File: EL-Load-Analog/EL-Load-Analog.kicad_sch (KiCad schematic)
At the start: 52 parts, among them J1 Fan PWM, J101 Conn_01x10_Male, J102 JST-XH 2-pin, J103 JST-XH 2-pin, J104 Conn_02x12_Counter_Clockwise, Q101 TIP42C, U1 ADS1115IDGS, U101 AMS1117-3.3, U102 ADM1032, U2 MAX31760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

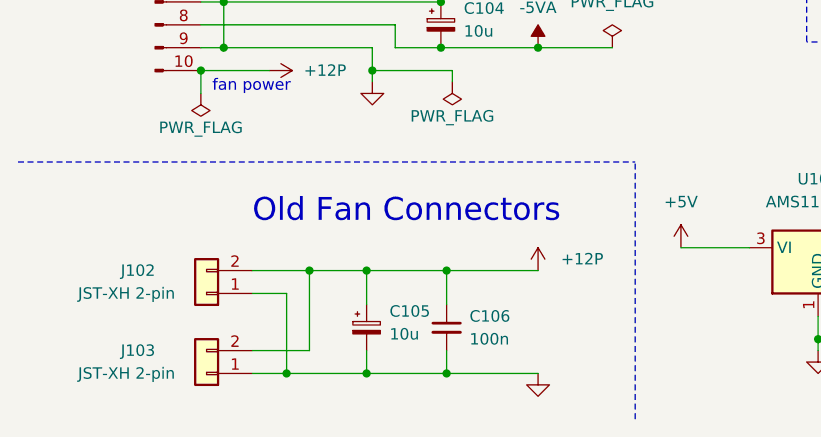
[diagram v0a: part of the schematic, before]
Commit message: Put REF2025 in place, added LICENSES and .gitignore
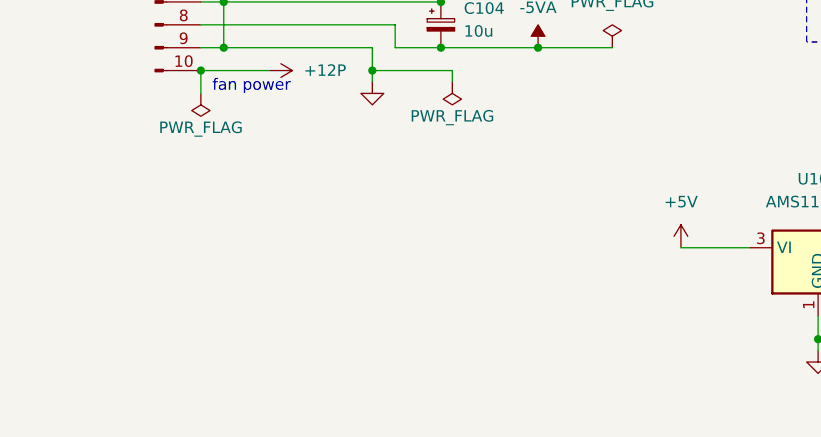
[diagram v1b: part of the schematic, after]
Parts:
- removed C105: 10u, Capacitor_SMD:C_0805_2012Metric_Pad1.18x1.45mm_HandSolder, symbol Device:C_Polarized_Small
- removed C106: 100n, Capacitor_SMD:C_0805_2012Metric_Pad1.18x1.45mm_HandSolder, symbol Device:C_Small
- removed J102, J103: JST-XH 2-pin, Connector_JST:JST_XH_B2B-XH-A_1x02_P2.50mm_Vertical, symbol Connector_Generic:Conn_01x02
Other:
- note removed: "Old Fan Connectors"

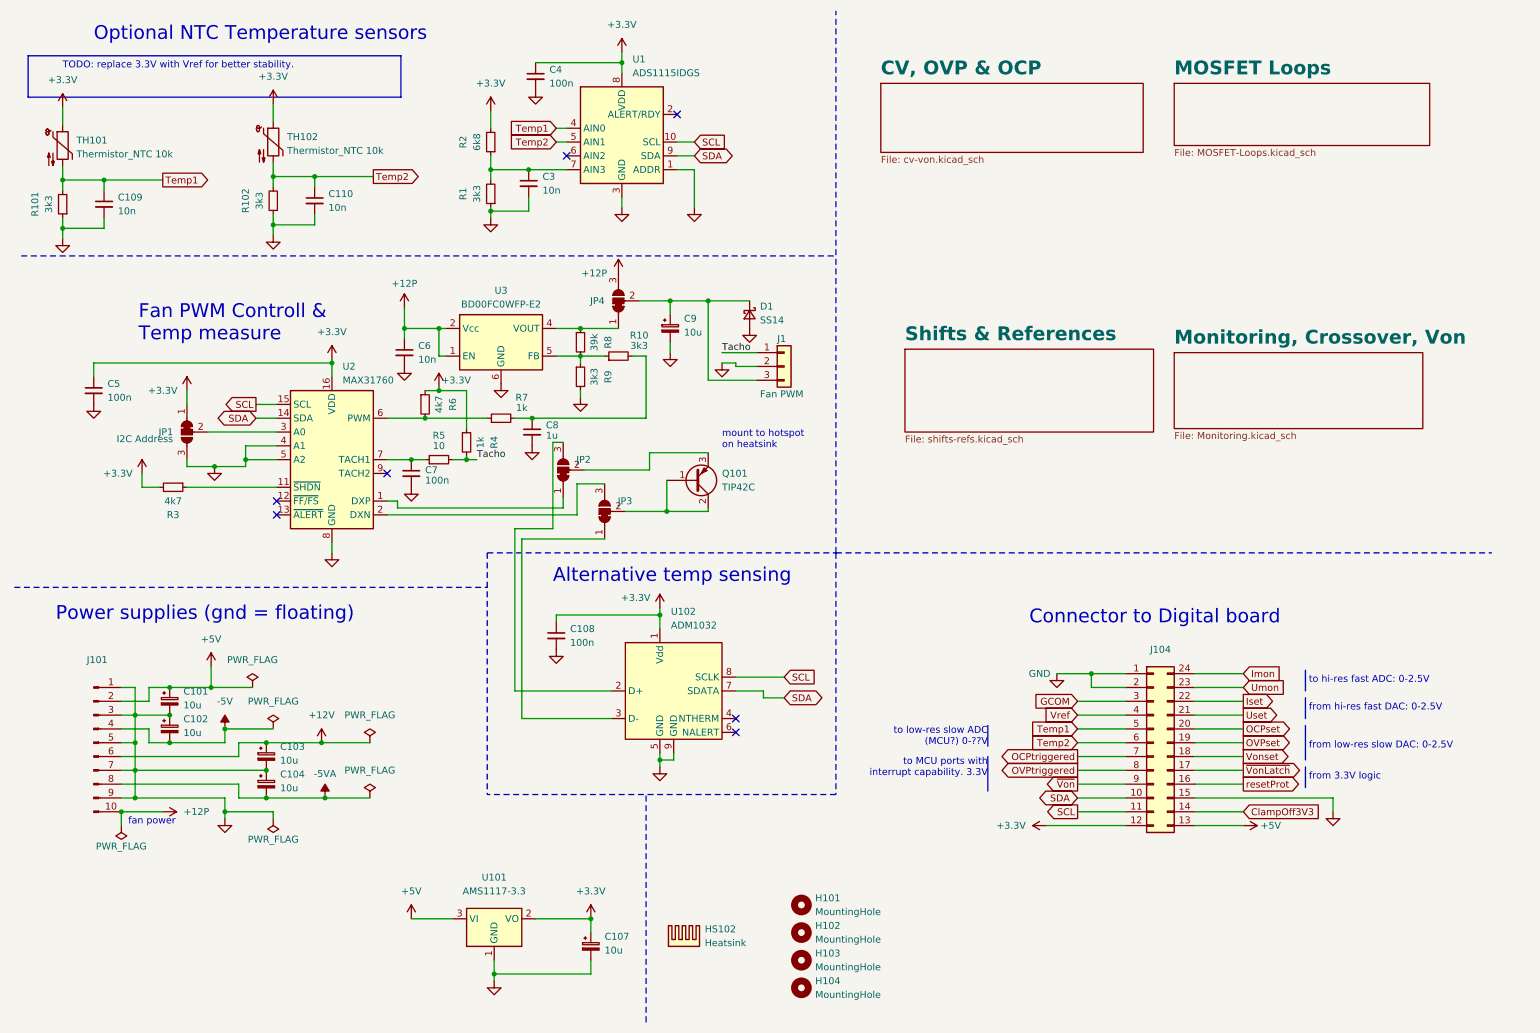
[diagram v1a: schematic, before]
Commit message: Major Analog PCB update DAC/ADC + connectors included, fan IC removed
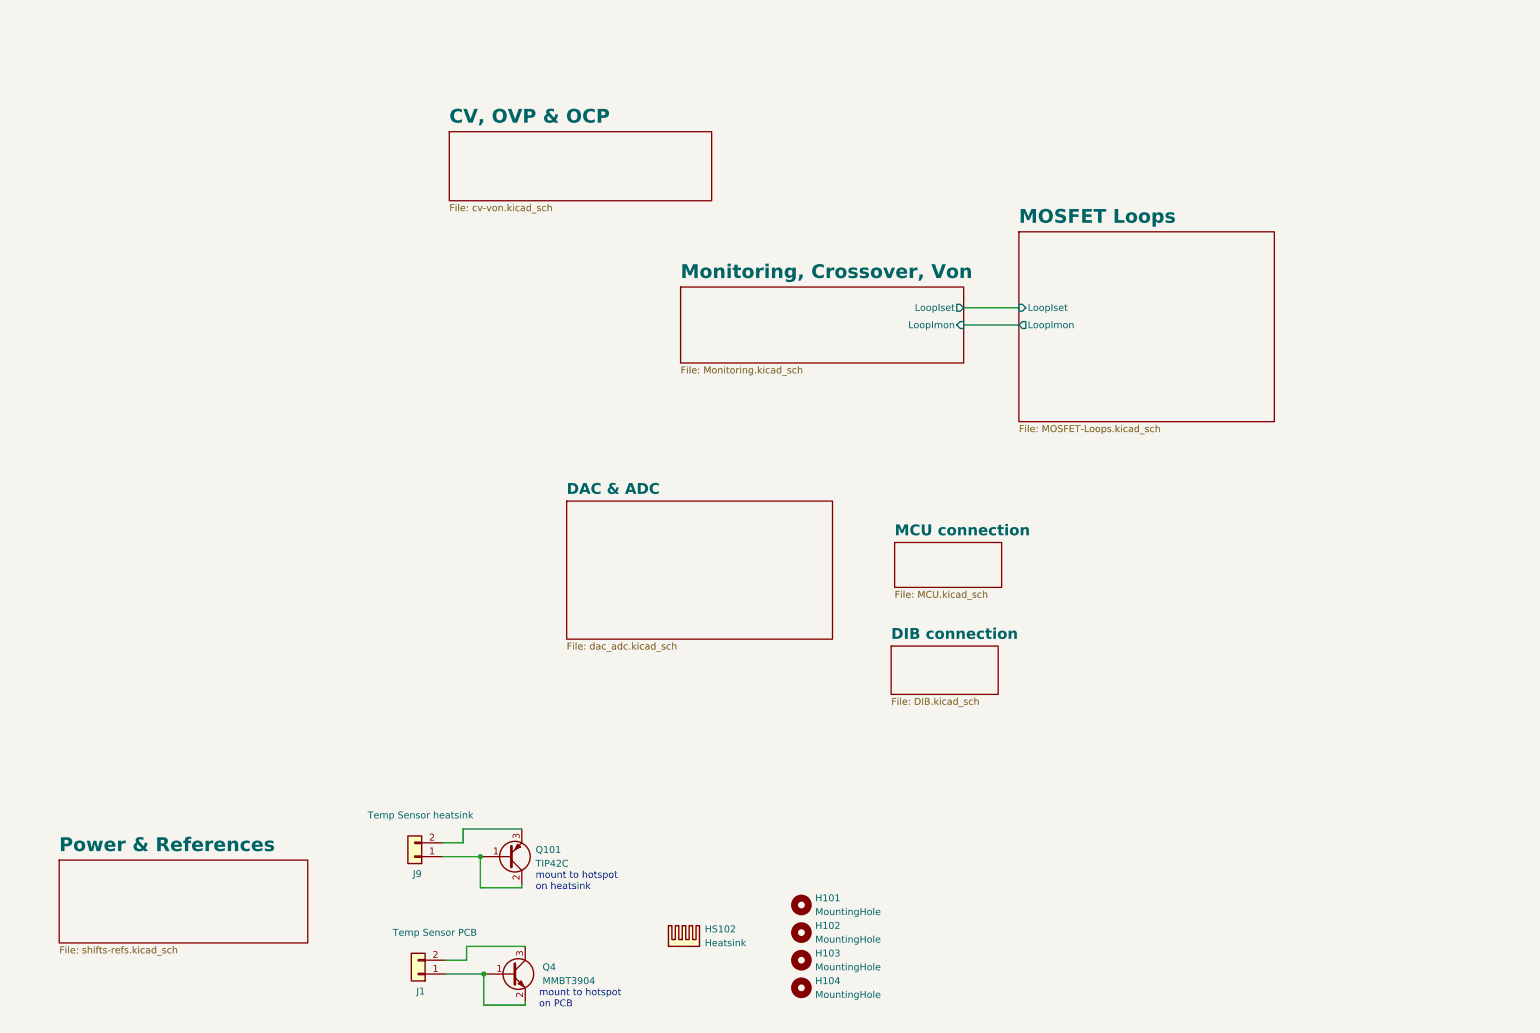
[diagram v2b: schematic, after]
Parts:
- removed C101, C102, C103, C104, C107: 10u, Capacitor_SMD:C_0805_2012Metric_Pad1.18x1.45mm_HandSolder, symbol Device:C_Polarized_Small
- removed C108, C4, C5, C7: 100n, Capacitor_SMD:C_0805_2012Metric_Pad1.18x1.45mm_HandSolder, symbol Device:C_Small
- removed C109, C110, C3, C6: 10n, Capacitor_SMD:C_0805_2012Metric_Pad1.18x1.45mm_HandSolder, symbol Device:C_Small
- removed C8: 1u, Capacitor_SMD:C_0805_2012Metric_Pad1.18x1.45mm_HandSolder, symbol Device:C_Small
- removed C9: 10u, Capacitor_SMD:CP_Elec_6.3x5.8, symbol Device:C_Polarized_Small
- removed D1: SS14, Diode_SMD:D_SMA_Handsoldering, symbol Device:D_Schottky_Small
- removed J1: Fan PWM, Connector_JST:JST_XH_B3B-XH-A_1x03_P2.50mm_Vertical, symbol Connector_Generic:Conn_01x03
- removed J101: Conn_01x10_Male, Connector_PinHeader_2.54mm:PinHeader_1x10_P2.54mm_Horizontal, symbol Connector:Conn_01x10_Pin
- removed J104: Conn_02x12_Counter_Clockwise, Connector_PinHeader_2.54mm:PinHeader_2x12_P2.54mm_Vertical, symbol Connector_Generic:Conn_02x12_Counter_Clockwise
- removed JP1: I2C Address, Jumper:SolderJumper-3_P1.3mm_Bridged2Bar12_RoundedPad1.0x1.5mm, symbol Jumper:SolderJumper_3_Bridged12
- removed JP2, JP3, JP4: SolderJumper_3_Bridged12, Jumper:SolderJumper-3_P1.3mm_Bridged2Bar12_RoundedPad1.0x1.5mm, symbol Jumper:SolderJumper_3_Bridged12
- removed R1, R10, R101, R102, R9: 3k3, Resistor_SMD:R_0805_2012Metric_Pad1.20x1.40mm_HandSolder, symbol Device:R_Small
- removed R2: 6k8, Resistor_SMD:R_0805_2012Metric_Pad1.20x1.40mm_HandSolder, symbol Device:R_Small
- removed R3, R6: 4k7, Resistor_SMD:R_0805_2012Metric_Pad1.20x1.40mm_HandSolder, symbol Device:R_Small
- removed R4, R7: 1k, Resistor_SMD:R_0805_2012Metric_Pad1.20x1.40mm_HandSolder, symbol Device:R_Small
- removed R5: 10, Resistor_SMD:R_0805_2012Metric_Pad1.20x1.40mm_HandSolder, symbol Device:R_Small
- removed R8: 39k, Resistor_SMD:R_0805_2012Metric_Pad1.20x1.40mm_HandSolder, symbol Device:R_Small
- removed TH101, TH102: Thermistor_NTC 10k, Connector_PinHeader_2.00mm:PinHeader_1x02_P2.00mm_Vertical, symbol Device:Thermistor_NTC
- removed U1: ADS1115IDGS, Package_SO:TSSOP-10_3x3mm_P0.5mm, symbol Analog_ADC:ADS1115IDGS
- removed U101: AMS1117-3.3, Package_TO_SOT_SMD:SOT-223-3_TabPin2, symbol Regulator_Linear:AMS1117-3.3
- removed U102: ADM1032, Package_SO:MSOP-8-1EP_3x3mm_P0.65mm_EP1.68x1.88mm, symbol EL-Load:ADM1032
- removed U2: MAX31760, Package_SO:QSOP-16_3.9x4.9mm_P0.635mm, symbol EL-Load:MAX31760
- removed U3: BD00FC0WFP-E2, Package_TO_SOT_SMD:TO-252-5_TabPin6, symbol EL-Load:BD00FC0W
- added J1: Temp Sensor PCB, Connector_JST:JST_XH_B2B-XH-A_1x02_P2.50mm_Vertical, symbol Connector_Generic:Conn_01x02
- added J9: Temp Sensor heatsink, Connector_JST:JST_XH_B2B-XH-A_1x02_P2.50mm_Vertical, symbol Connector_Generic:Conn_01x02
- added Q4: MMBT3904, Package_TO_SOT_SMD:SOT-23, symbol Transistor_BJT:MMBT3904
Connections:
- net at Q101.1 (B), Q101.2 (C): now also J9.1 (Pin_1)
- net at Q101.3 (E): now also J9.2 (Pin_2)
- new net: J1.1 (Pin_1), Q4.1 (B), Q4.2 (E)
- new net: J1.2 (Pin_2), Q4.3 (C)
- no-connect marks 7 -> 0
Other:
- sheet Shifts & References renamed Power & References
- added sheet DAC & ADC (dac_adc.kicad_sch)
- added sheet DIB connection (DIB.kicad_sch)
- added sheet MCU connection (MCU.kicad_sch)
- sheet MOSFET Loops ports: added LoopImon, LoopIset; removed none
- sheet Monitoring, Crossover, Von ports: added LoopImon, LoopIset; removed none
- note added: "mount to hotspot on PCB"
- note removed: "Alternative temp sensing"
- note removed: "Connector to Digital board"
- note removed: "Fan PWM Controll & Temp measure"
- note removed: "Optional NTC Temperature sensors"
- note removed: "Power supplies (gnd = floating)"
- note removed: "TODO: replace 3.3V with Vref for better stability."
- note removed: "fan power"
- note removed: "from 3.3V logic"
- note removed: "from hi-res fast DAC: 0-2.5V"
- note removed: "from low-res slow DAC: 0-2.5V"
- note removed: "to MCU ports with interrupt capability. 3.3V"
- note removed: "to hi-res fast ADC: 0-2.5V"
- note removed: "to low-res slow ADC (MCU?) 0-??V"
- moved on the sheet: Q101

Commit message: Added SenseError detection (including ocmponents), added clearances, fixed few BOM items.
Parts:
- H101, H102, H103, H104: footprint MountingHole:MountingHole_3.2mm_M3_DIN965_Pad -> MountingHole:MountingHole_3.2mm_M3_DIN965
- J1, J9: Part Name (none) -> H_JST_XH_PCB_2P_VERT
- Q4: Part Name (none) -> Q_MMBT3904
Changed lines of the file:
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@@
       (effects (font (size 1.27 1.27)) (justify left))
     )
-    (property "Footprint" "MountingHole:MountingHole_3.2mm_M3_DIN965_Pad" (at 157.48 176.53 0)
+    (property "Footprint" "MountingHole:MountingHole_3.2mm_M3_DIN965" (at 157.48 176.53 0)
       (effects (font (size 1.27 1.27)) hide)
     )
@@
       (effects (font (size 1.27 1.27)) hide)
     )
+    (property "Part Name" "H_JST_XH_PCB_2P_VERT " (at 86.36 167.64 0)
+      (effects (font (size 1.27 1.27)) hide)
+    )
     (pin "1")
     (pin "2")
@@
       (effects (font (size 1.27 1.27)) (justify left))
     )
-    (property "Footprint" "MountingHole:MountingHole_3.2mm_M3_DIN965_Pad" (at 157.48 181.61 0)
+    (property "Footprint" "MountingHole:MountingHole_3.2mm_M3_DIN965" (at 157.48 181.61 0)
       (effects (font (size 1.27 1.27)) hide)
     )
@@
       (effects (font (size 1.27 1.27)) (justify left) hide)
     )
+    (property "Part Name" "Q_MMBT3904" (at 104.14 189.23 0)
+      (effects (font (size 1.27 1.27)) hide)
+    )
     (pin "1")
     (pin "2")
@@
       (effects (font (size 1.27 1.27)) (justify left))
     )
-    (property "Footprint" "MountingHole:MountingHole_3.2mm_M3_DIN965_Pad" (at 157.48 186.69 0)
+    (property "Footprint" "MountingHole:MountingHole_3.2mm_M3_DIN965" (at 157.48 186.69 0)
       (effects (font (size 1.27 1.27)) hide)
     )
@@
       (effects (font (size 1.27 1.27)) (justify left))
     )
-    (property "Footprint" "MountingHole:MountingHole_3.2mm_M3_DIN965_Pad" (at 157.48 191.77 0)
+    (property "Footprint" "MountingHole:MountingHole_3.2mm_M3_DIN965" (at 157.48 191.77 0)
       (effects (font (size 1.27 1.27)) hide)
     )
@@
       (effects (font (size 1.27 1.27)) hide)
     )
+    (property "Part Name" "H_JST_XH_PCB_2P_VERT " (at 86.995 189.23 0)
+      (effects (font (size 1.27 1.27)) hide)
+    )
